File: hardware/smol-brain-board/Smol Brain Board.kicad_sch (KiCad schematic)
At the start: 59 parts, among them J1 USB4085-GF-A, J3 CAN_DBG, J6 Smol_Brain_Board, J7 PROGRAM, J8 Jumper 2Way Vert Solderable, J9 Jumper 2Way Vert Solderable, U1 ESP32-S3-WROOM-1-N8, U3 SN65HVD231D

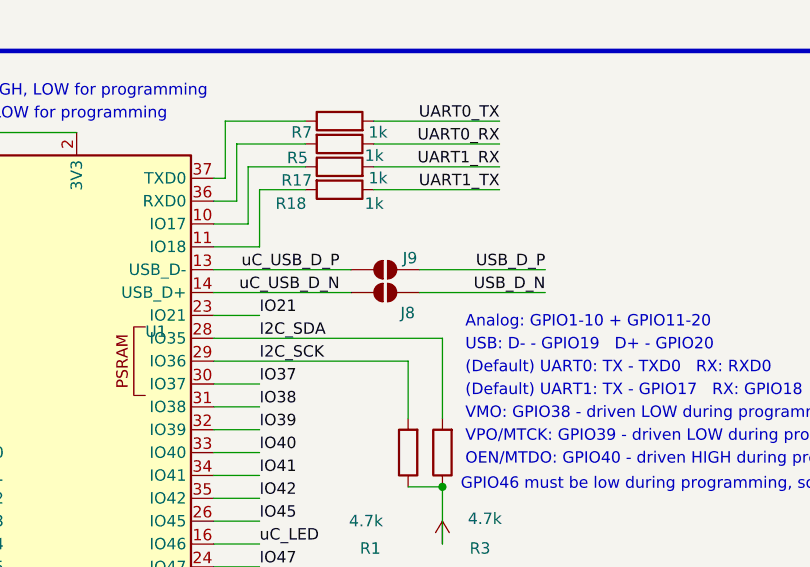
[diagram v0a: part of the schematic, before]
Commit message: Fixed impedance matching for USB and decoupling cap placement
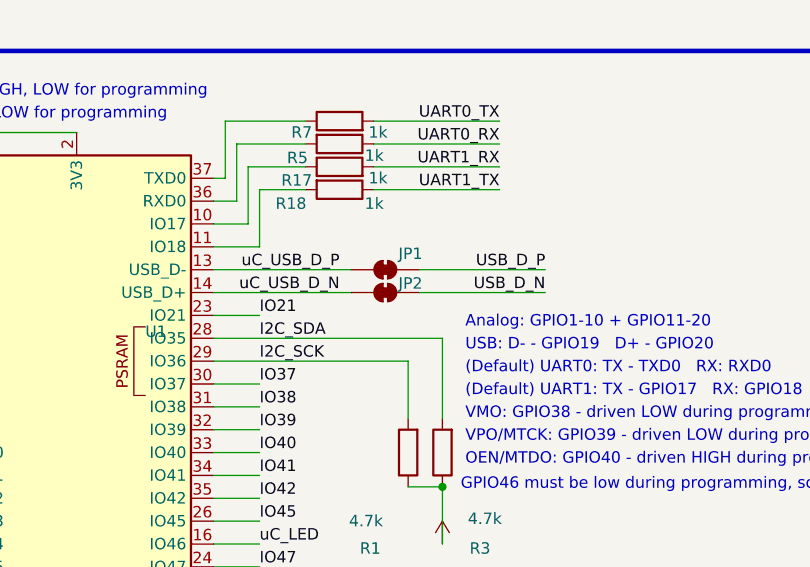
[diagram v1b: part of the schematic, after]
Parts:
- removed J8, J9: Jumper 2Way Vert Solderable, Jumper:SolderJumper-2_P1.3mm_Open_RoundedPad1.0x1.5mm, symbol Jumper:SolderJumper_2_Open
- added JP1, JP2: SolderJumper_2_Bridged, Jumper:SolderJumper-2_P1.3mm_Bridged_RoundedPad1.0x1.5mm, symbol Jumper:SolderJumper_2_Bridged
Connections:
- net USB_D_N: now also JP2.2 (B)
- net USB_D_P: now also JP1.2 (B)
- net uC_USB_D_N: now also JP2.1 (A)
- net uC_USB_D_P: now also JP1.1 (A)
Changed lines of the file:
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@@
 	(label "USB_D_N"
 		(at 359.41 48.26 180)
+		(fields_autoplaced yes)
 		(effects
 			(font
@@
 			(justify right bottom)
 		)
+		(property "Netclass" "USB_DIFF"
+			(at 359.41 49.53 0)
+			(effects
+				(font
+					(size 1.27 1.27)
+					(italic yes)
+				)
+				(justify right)
+				(hide yes)
+			)
+		)
 	)
 	(label "CAN_TX"
@@
 			(justify right bottom)
 		)
+		(property "Netclass" "USB_DIFF"
+			(at 337.058 42.672 0)
+			(effects
+				(font
+					(size 1.27 1.27)
+					(italic yes)
+				)
+				(justify right)
+				(hide yes)
+			)
+		)
 	)
 	(label "IO40"
@@
 	(label "USB_D_N"
 		(at 168.91 74.93 0)
+		(fields_autoplaced yes)
 		(effects
 			(font
@@
 			(justify left bottom)
 		)
+		(property "Netclass" "USB_DIFF"
+			(at 168.91 76.2 0)
+			(effects
+				(font
+					(size 1.27 1.27)
+					(italic yes)
+				)
+				(justify left)
+			)
+		)
 	)
 	(label "A4"
@@
 	(label "USB_D_P"
 		(at 359.41 45.72 180)
+		(fields_autoplaced yes)
 		(effects
 			(font
@@
 			(justify right bottom)
 		)
+		(property "Netclass" "USB_DIFF"
+			(at 359.41 46.99 0)
+			(effects
+				(font
+					(size 1.27 1.27)
+					(italic yes)
+				)
+				(justify right)
+				(hide yes)
+			)
+		)
 	)
 	(label "RST"
@@
 	(label "uC_USB_D_N"
 		(at 336.55 48.26 180)
+		(fields_autoplaced yes)
 		(effects
 			(font
@@
 			(justify right bottom)
 		)
+		(property "Netclass" "USB_DIFF"
+			(at 336.55 49.53 0)
+			(effects
+				(font
+					(size 1.27 1.27)
+					(italic yes)
+				)
+				(justify right)
+				(hide yes)
+			)
+		)
 	)
 	(label "CAN_H"
@@
 	(label "USB_D_P"
 		(at 168.91 80.01 0)
+		(fields_autoplaced yes)
 		(effects
 			(font
@@
 			(justify left bottom)
 		)
+		(property "Netclass" "USB_DIFF"
+			(at 168.91 81.28 0)
+			(effects
+				(font
+					(size 1.27 1.27)
+					(italic yes)
+				)
+				(justify left)
+			)
+		)
 	)
 	(label "IO15"
@@
 	)
 	(symbol
-		(lib_id "Jumper:SolderJumper_2_Open")
-		(at 341.63 45.72 180)
-		(unit 1)
-		(exclude_from_sim no)
-		(in_bom no)
-		(on_board yes)
-		(dnp no)
-		(property "Reference" "J9"
-			(at 345.186 43.688 0)
-			(effects
-				(font
-					(size 1.27 1.27)
-				)
-				(justify left bottom)
-			)
-		)
-		(property "Value" "Jumper 2Way Vert Solderable"
-			(at 349.758 46.99 0)
-			(effects
-				(font
-					(size 1.27 1.27)
-				)
-				(justify left bottom)
-				(hide yes)
-			)
-		)
-		(property "Footprint" "Jumper:SolderJumper-2_P1.3mm_Open_RoundedPad1.0x1.5mm"
-			(at 341.63 45.72 0)
-			(effects
-				(font
-					(size 1.27 1.27)
-				)
-				(hide yes)
-			)
-		)
-		(property "Datasheet" "~"
-			(at 341.63 45.72 0)
-			(effects
-				(font
-					(size 1.27 1.27)
-				)
-				(hide yes)
-			)
-		)
-		(property "Description" "Solder Jumper, 2-pole, open"
-			(at 341.63 45.72 0)
-			(effects
-				(font
-					(size 1.27 1.27)
-				)
-				(hide yes)
-			)
-		)
-		(property "SOURCE" "QUTMS_JumperLibrary.SchLib"
-			(at 349.758 46.99 0)
-			(effects
-				(font
-					(size 1.27 1.27)
-				)
-				(justify left bottom)
-				(hide yes)
-			)
-		)
-		(property "DESIGN ITEM ID" "Jumper 2Way Vert Solderable"
-			(at 349.758 46.99 0)
-			(effects
-				(font
-					(size 1.27 1.27)
-				)
-				(justify left bottom)
-				(hide yes)
-			)
-		)
-		(pin "1"
-		)
-		(pin "2"
-		)
-		(instances
-			(project ""
-				(path "/d947cca5-df2f-4130-8179-c021102beaa2"
-					(reference "J9")
-					(unit 1)
-				)
-			)
-		)
-	)
-	(symbol
 		(lib_id "power:GND")
 		(at 182.88 67.31 90)
@@
 	)
 	(symbol
-		(lib_id "Jumper:SolderJumper_2_Open")
-		(at 341.63 48.26 180)
+		(lib_id "Jumper:SolderJumper_2_Bridged")
+		(at 341.63 48.26 0)
 		(unit 1)
 		(exclude_from_sim no)
@@
 		(on_board yes)
 		(dnp no)
-		(property "Reference" "J8"
-			(at 344.932 49.784 0)
+		(property "Reference" "JP2"
+			(at 344.424 47.244 0)
 			(effects
 				(font
 					(size 1.27 1.27)
 				)
-				(justify left bottom)
 			)
 		)
-		(property "Value" "Jumper 2Way Vert Solderable"
-			(at 349.758 49.53 0)
+		(property "Value" "SolderJumper_2_Bridged"
+			(at 341.63 44.45 0)
 			(effects
 				(font
 					(size 1.27 1.27)
 				)
-				(justify left bottom)
 				(hide yes)
 			)
 		)
-		(property "Footprint" "Jumper:SolderJumper-2_P1.3mm_Open_RoundedPad1.0x1.5mm"
+		(property "Footprint" "Jumper:SolderJumper-2_P1.3mm_Bridged_RoundedPad1.0x1.5mm"
 			(at 341.63 48.26 0)
 			(effects
@@
 			)
 		)
-		(property "Description" "Solder Jumper, 2-pole, open"
+		(property "Description" "Solder Jumper, 2-pole, closed/bridged"
 			(at 341.63 48.26 0)
 			(effects
@@
 			)
 		)
-		(property "SOURCE" "QUTMS_JumperLibrary.SchLib"
-			(at 349.758 49.53 0)
-			(effects
-				(font
-					(size 1.27 1.27)
-				)
-				(justify left bottom)
-				(hide yes)
-			)
-		)
-		(property "DESIGN ITEM ID" "Jumper 2Way Vert Solderable"
-			(at 349.758 49.53 0)
-			(effects
-				(font
-					(size 1.27 1.27)
-				)
-				(justify left bottom)
-				(hide yes)
-			)
+		(pin "2"
 		)
 		(pin "1"
 		)
-		(pin "2"
-		)
 		(instances
-			(project ""
+			(project "Smol Brain Board"
 				(path "/d947cca5-df2f-4130-8179-c021102beaa2"
-					(reference "J8")
+					(reference "JP2")
 					(unit 1)
 				)
@@
 					(unit 1)
 				)
+			)
+		)
+	)
+	(symbol
+		(lib_id "Jumper:SolderJumper_2_Bridged")
+		(at 341.63 45.72 0)
+		(unit 1)
+		(exclude_from_sim no)
+		(in_bom no)
+		(on_board yes)
+		(dnp no)
+		(property "Reference" "JP1"
+			(at 344.424 43.942 0)
+			(effects
+				(font
+					(size 1.27 1.27)
+				)
+			)
+		)
+		(property "Value" "SolderJumper_2_Bridged"
+			(at 341.63 41.91 0)
+			(effects
+				(font
+					(size 1.27 1.27)
+				)
+				(hide yes)
+			)
+		)
+		(property "Footprint" "Jumper:SolderJumper-2_P1.3mm_Bridged_RoundedPad1.0x1.5mm"
+			(at 341.63 45.72 0)
+			(effects
+				(font
+					(size 1.27 1.27)
+				)
+				(hide yes)
+			)
+		)
+		(property "Datasheet" "~"
+			(at 341.63 45.72 0)
+			(effects
+				(font
+					(size 1.27 1.27)
+				)
+				(hide yes)
+			)
+		)
+		(property "Description" "Solder Jumper, 2-pole, closed/bridged"
+			(at 341.63 45.72 0)
+			(effects
+				(font
+					(size 1.27 1.27)
+				)
+				(hide yes)
+			)
+		)
+		(pin "2"
+		)
+		(pin "1"
+		)
+		(instances
+			(project ""
+				(path "/d947cca5-df2f-4130-8179-c021102beaa2"
+					(reference "JP1")
+					(unit 1)
+				)

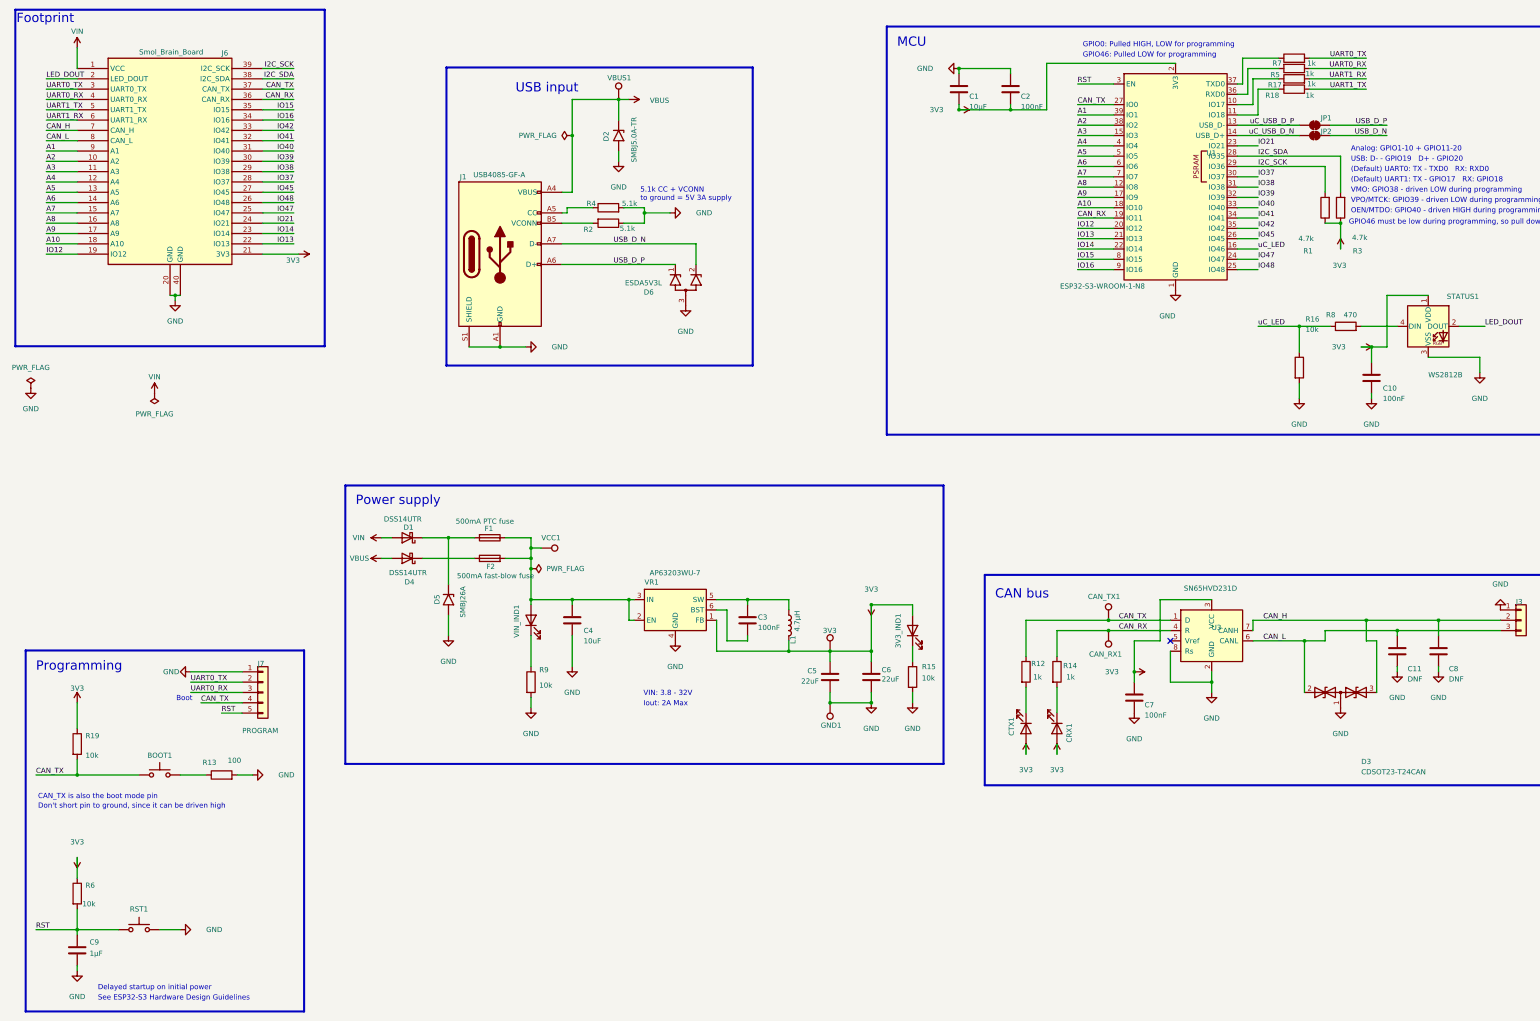
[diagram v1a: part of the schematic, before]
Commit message: Added real world components and finalised PCB, ready for manufacturing
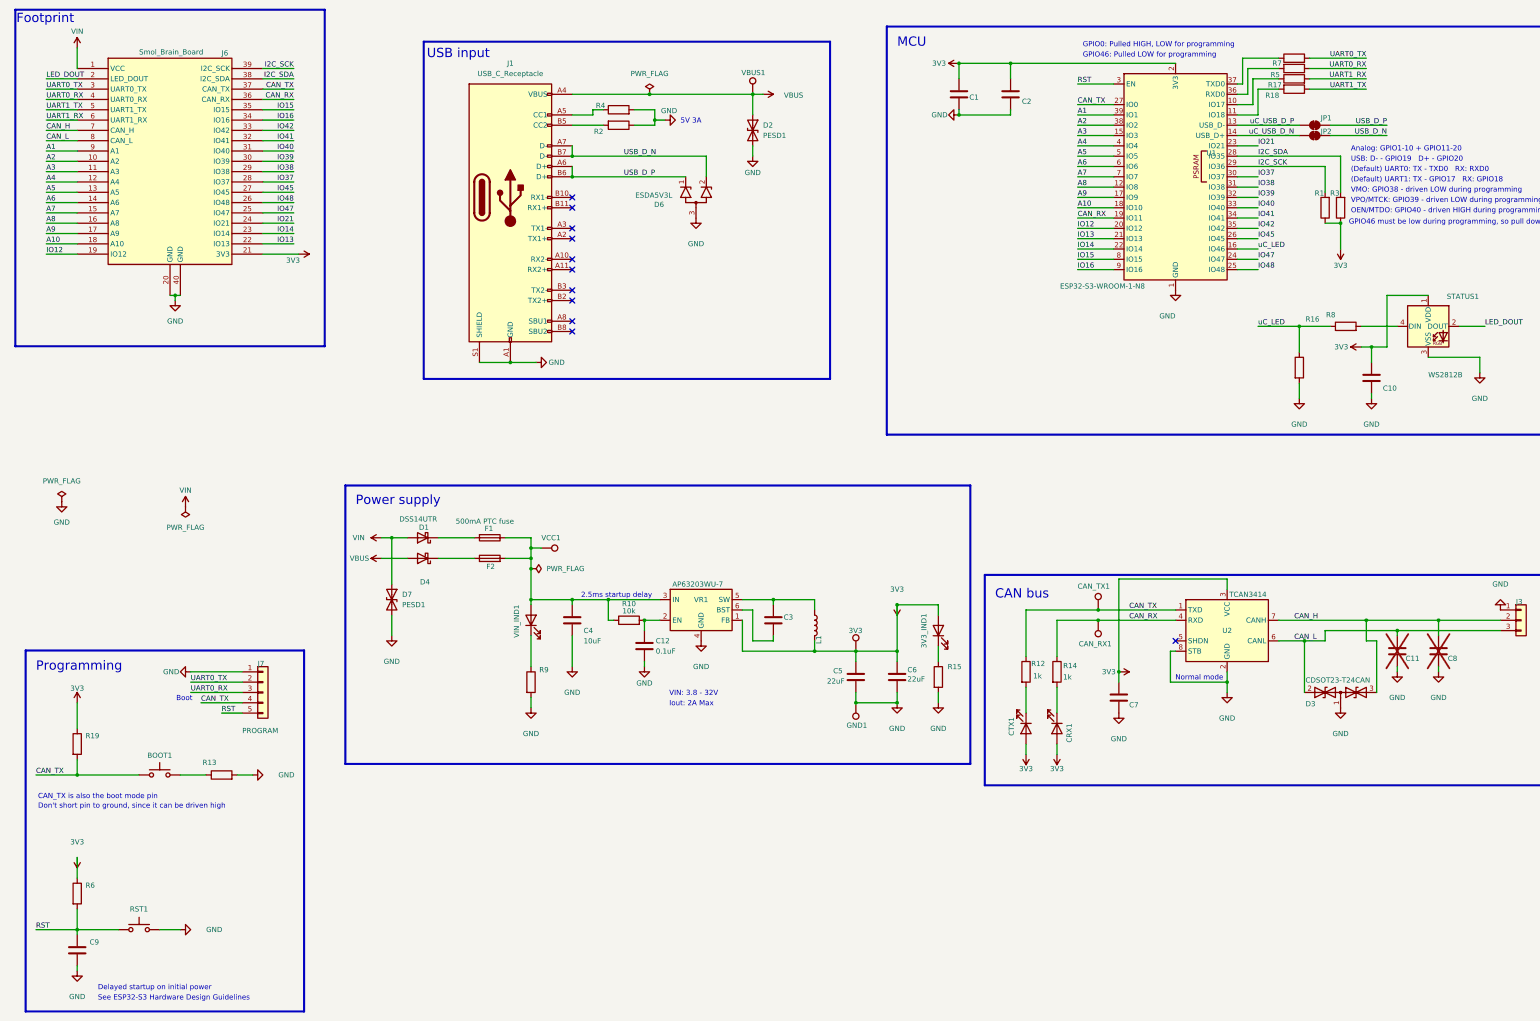
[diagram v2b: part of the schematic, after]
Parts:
- removed D2: SMBJ5.0A-TR, Diode_SMD:D_SMA, symbol Diode:SMAJ6.5A
- removed D5: SMBJ26A, Diode_SMD:D_SMA, symbol Diode:SMAJ26A
- removed J1: USB4085-GF-A, Connector_USB:USB_C_Receptacle_GCT_USB4085, symbol Connector:USB_C_Plug_USB2.0
- removed U3: SN65HVD231D, Package_SO:SOIC-8_3.9x4.9mm_P1.27mm, symbol Interface_CAN_LIN:SN65HVD231
- added C12: 0.1uF, Capacitor_SMD:C_0402_1005Metric, symbol Device:C
- added D2, D7: PESD1, Diode_SMD:D_SOD-882, symbol Device:D_TVS
- added J1: USB_C_Receptacle, Connector_USB:USB_C_Receptacle_Amphenol_12401610E4-2A, symbol Connector:USB_C_Receptacle
- added R10: 10k, Resistor_SMD:R_0402_1005Metric, symbol Device:R
- added U2: TCAN3414, Library:TCAN3414, symbol component_library:TCAN3414DDFR
- 3V3, CAN_RX1, CAN_TX1, GND1, VBUS1, VCC1: DESIGN ITEM ID Testpoint -> (none); SOURCE Testpoint.SchLib -> (none)
- 3V3_IND1, VIN_IND1: CASE/PACKAGE 0603 -> (none); COLOUR Red -> (none); DATASHEET URL http://optoelectronics.liteon.com/upload/download/DS-22-99-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 -> (none); DATASHEET VERSION Rev. F, 05/2013 -> (none); FORWARD CURRENT 20mA -> (none); FORWARD VOLTAGE 2V -> (none); ILLUMINATION COLOUR Red -> (none); LENS STYLE Diffused -> (none); LUMINOUS INTENSITY 54mcd -> (none); MANUFACTURER Lite-On -> (none); MANUFACTURER URL http://www.us.liteon.com/ -> (none); MAX OPERATING TEMPERATURE 85°C -> (none); MIN OPERATING TEMPERATURE -55°C -> (none); MOUNTING TECHNOLOGY SM -> (none); NOMINAL VF 2V -> (none); PACKAGE DESCRIPTION 2-Pin Surface Mount Device, Body 1.6 x 0.8 mm -> (none); PACKAGE QUANTITY 3000 -> (none); PACKAGE REFERENCE C191KRKT -> (none); PACKAGING TapeandReel -> (none); PINS 2 -> (none); POWER 75mW -> (none); ROHS COMPLIANT True -> (none); VIEWING ANGLE 130degrees -> (none); distributors part number (none) -> 160-1436-2-ND; manufactuer part number (none) -> LTST-C190KRKT; manufacturer (none) -> Lite-On Inc
- BOOT1, RST1: distributors part number (none) -> CKN12324-2-ND; manufactuer part number (none) -> GSPTS004302; manufacturer (none) -> C&K
- C1: ALTIUM_VALUE 10µF -> (none); CAPACITOR TYPE Ceramic -> (none); CASE/PACKAGE 0805 -> (none); DIELECTRIC MATERIAL Ceramic -> (none); HEIGHT 1.4mm -> (none); JESD-609 CODE e3 -> (none); LENGTH 2mm -> (none); MAX OPERATING TEMPERATURE 85°C -> (none); MIN OPERATING TEMPERATURE -55°C -> (none); MOUNTING TECHNOLOGY Surface Mount -> (none); MULTILAYER Yes -> (none); PACKAGE SHAPE Rectangular -> (none); PACKAGE STYLE SMTMeter -> (none); PACKAGING Tape and Reel -> (none); PINS 2 -> (none); RATED DC VOLTAGE (URDC) 16V -> (none); REACH SVHC COMPLIANT Yes -> (none); ROHS COMPLIANT Yes -> (none); TEMPERATURE CHARACTERISTICS CODE X5R -> (none); TERMINAL FINISH Nickel -> (none); TERMINATION Wraparound -> (none); TOLERANCE  (FILL IN AS +-) 10% -> (none); TOLERANCE (FILL IN AS +-) 10% -> (none); VOLTAGE RATING 16V -> (none); WIDTH 1.25mm -> (none); distributors part number (none) -> 1276-2872-2-ND; manufactuer part number (none) -> CL21B106KOQNNNE; manufacturer (none) -> Samsung Electro-Mechanics
- C10, C2, C3, C7: ALTIUM_VALUE 100nF -> (none); CAPACITOR TYPE Ceramic -> (none); CASE/PACKAGE 0603 -> (none); DIELECTRIC MATERIAL Ceramic -> (none); JESD-609 CODE e3 -> (none); MAX OPERATING TEMPERATURE 125°C -> (none); MIN OPERATING TEMPERATURE -55°C -> (none); MOUNTING TECHNOLOGY Surface Mount -> (none); MULTILAYER Yes -> (none); PACKAGE SHAPE Rectangular -> (none); PACKAGING Tape and Reel -> (none); PINS 2 -> (none); RATED DC VOLTAGE (URDC) 50V -> (none); REACH SVHC COMPLIANT Yes -> (none); ROHS COMPLIANT Yes -> (none); TEMPERATURE CHARACTERISTICS CODE X7R -> (none); TERMINAL FINISH Nickel -> (none); TERMINATION Wraparound -> (none); TOLERANCE  (FILL IN AS +-) 10% -> (none); TOLERANCE (FILL IN AS +-) 10% -> (none); VOLTAGE RATING 50V -> (none); distributors part number (none) -> 1276-1012-2-ND; manufactuer part number (none) -> CL10F104ZB8NNNC; manufacturer (none) -> Samsung Electro-Mechanics
- C11, C8: CAPACITOR TYPE Ceramic -> (none); CASE/PACKAGE 0603 -> (none); DNF DNF -> (none); MAX OPERATING TEMPERATURE 85°C -> (none); MIN OPERATING TEMPERATURE -55°C -> (none); MOUNTING TECHNOLOGY Surface Mount -> (none); PINS 2 -> (none); now not fitted
- C4: CAPACITANCE 10uF -> (none); CASE/PACKAGE 0603 -> (none); MAX OPERATING TEMPERATURE 85°C -> (none); MIN OPERATING TEMPERATURE -55°C -> (none); MOUNT Surface Mount -> (none); PACKAGING Tape and Reel -> (none); TOLERANCE 20% -> (none); VOLTAGE RATING 35V -> (none); distributors part number (none) -> 1276-1192-2-ND; manufactuer part number (none) -> CL10A106KP8NNNC; manufacturer (none) -> Samsung Electro-Mechanics
- C5, C6: CAPACITANCE 22uF -> (none); CASE CODE (IMPERIAL) 0805 -> (none); CASE CODE (METRIC) 2012 -> (none); CASE/PACKAGE 0805 -> (none); CONTACT PLATING Tin -> (none); DEPTH 1.25mm -> (none); DIELECTRIC X5R -> (none); HEIGHT 1.25mm -> (none); LEAD FREE Lead Free -> (none); LENGTH 2mm -> (none); MAX OPERATING TEMPERATURE 85°C -> (none); MIN OPERATING TEMPERATURE -55°C -> (none); MOUNT Surface Mount -> (none); PACKAGE QUANTITY 2000 -> (none); PACKAGING Tape and Reel -> (none); RADIATION HARDENING No -> (none); THICKNESS 0.055inch -> (none); TOLERANCE 20% -> (none); VOLTAGE RATING 6.3V -> (none); VOLTAGE RATING (DC) 6.3V -> (none); WIDTH 0.049inch -> (none); distributors part number (none) -> 1276-1274-2-ND; manufactuer part number (none) -> CL10A226MP8NUNE; manufacturer (none) -> Samsung Electro-Mechanics
- C9: value Capacitor 1u 25V 0603 -> Capacitor 1u 25V; ALTIUM_VALUE 1µF -> (none); CAPACITOR TYPE Ceramic -> (none); CASE/PACKAGE 0603 -> (none); DIELECTRIC MATERIAL Ceramic -> (none); HEIGHT 0.9mm -> (none); JESD-609 CODE e3 -> (none); LENGTH 1.6mm -> (none); MAX OPERATING TEMPERATURE 85°C -> (none); MIN OPERATING TEMPERATURE -55°C -> (none); MOUNTING TECHNOLOGY Surface Mount -> (none); MULTILAYER Yes -> (none); PACKAGE SHAPE Rectangular -> (none); PACKAGE STYLE SMTMeter -> (none); PACKAGING Tape and Reel -> (none); PINS 2 -> (none); RATED DC VOLTAGE (URDC) 25V -> (none); REACH SVHC COMPLIANT Yes -> (none); ROHS COMPLIANT Yes -> (none); TEMPERATURE CHARACTERISTICS CODE X5R -> (none); TERMINAL FINISH Nickel -> (none); TERMINATION Wraparound -> (none); TOLERANCE  (FILL IN AS +-) 10% -> (none); TOLERANCE (FILL IN AS +-) 10% -> (none); WIDTH 0.8mm -> (none); distributors part number (none) -> 1276-1184-2-ND; manufactuer part number (none) -> CL10B105KA8NNNC; manufacturer (none) -> Samsung Electro-Mechanics
- CRX1: footprint LED_SMD:LED_0603_1608Metric -> LED_SMD:LED_0402_1005Metric; CASE/PACKAGE 0603 -> (none); COLOUR Green -> (none); DATASHEET URL http://datasheet.octopart.com/LTST-C190GKT-Lite-On-datashee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 -> (none); DATASHEET VERSION Dec-06 -> (none); FORWARD CURRENT 20mA -> (none); FORWARD VOLTAGE 2.1V -> (none); ILLUMINATION COLOUR Green -> (none); LENS STYLE Clear -> (none); LUMINOUS INTENSITY 6mcd -> (none); MANUFACTURER Lite-On -> (none); MANUFACTURER URL http://www.us.liteon.com/ -> (none); MAX OPERATING TEMPERATURE 85°C -> (none); MIN OPERATING TEMPERATURE -55°C -> (none); MOUNTING TECHNOLOGY SM -> (none); NOMINAL VF 2.1V -> (none); PACKAGE DESCRIPTION 2-Pin Surface Mount Device, Body 1.6 x 0.8 mm -> (none); PACKAGE QUANTITY 3000 -> (none); PACKAGE REFERENCE C190GKT -> (none); PACKAGING TapeandReel -> (none); PINS 2 -> (none); POWER 100mW -> (none); ROHS COMPLIANT True -> (none); VIEWING ANGLE 130degrees -> (none); distributors part number (none) -> 160-1436-2-ND; manufactuer part number (none) -> LTST-C190KRKT; manufacturer (none) -> Lite-On Inc
- CTX1: footprint LED_SMD:LED_0603_1608Metric -> LED_SMD:LED_0402_1005Metric; CASE/PACKAGE 0603 -> (none); COLOUR Yellow -> (none); DATASHEET URL http://optoelectronics.liteon.com/upload/download/DS-22-99-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 -> (none); DATASHEET VERSION Rev. I, 10/2012 -> (none); FORWARD CURRENT 20mA -> (none); FORWARD VOLTAGE 2V -> (none); ILLUMINATION COLOUR Yellow -> (none); LENS STYLE Diffused -> (none); LUMINOUS INTENSITY 28mcd -> (none); MANUFACTURER Lite-On -> (none); MANUFACTURER URL http://www.us.liteon.com/ -> (none); MAX OPERATING TEMPERATURE 85°C -> (none); MIN OPERATING TEMPERATURE -55°C -> (none); MOUNTING TECHNOLOGY SM -> (none); NOMINAL VF 2.1V -> (none); PACKAGE DESCRIPTION 2-Pin Surface Mount Device, Body 1.6 x 0.8 mm -> (none); PACKAGE QUANTITY 3000 -> (none); PACKAGE REFERENCE C190KSKT -> (none); PACKAGING TapeandReel -> (none); PINS 2 -> (none); POWER 75mW -> (none); ROHS COMPLIANT True -> (none); VIEWING ANGLE 130degrees -> (none); distributors part number (none) -> 160-1436-2-ND; manufactuer part number (none) -> LTST-C190KRKT; manufacturer (none) -> Lite-On Inc
- D1, D4: ALTIUM_VALUE * -> (none); AVAILABILITY In Stock -> (none); CASE/PACKAGE SOD-123F SMC Diode Solutions -> (none); CHECK_PRICES https://www.snapeda.com/parts/DSS14UTR/SMC+Diode+Solutions/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 -> (none); DESIGN ITEM ID DSS14UTR -> (none); MF SMC Diode Solutions -> (none); MP DSS14UTR -> (none); PRICE None -> (none); PURCHASE-URL https://pricing.snapeda.com/search/part/DSS14UTR/?ref=eda -> (none); SNAPEDA_LINK https://www.snapeda.com/parts/DSS14UTR/SMC+Diode+Solutions/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 -> (none); SOURCE DSS14UTR.SchLib -> (none); distributors part number (none) -> 1655-DSS14UTR-ND; manufactuer part number (none) -> DSS14U; manufacturer (none) -> SMC Diode Solutions
- D3: ALTIUM_VALUE 22pF -> (none); AUTOMOTIVE No -> (none); BREAKDOWN VOLTAGE 26.2V -> (none); CAPACITANCE 22pF -> (none); CATEGORY Diode -> (none); CLAMPING VOLTAGE 40V -> (none); COMPONENTLINK2DESCRIPTION Datasheet -> (none); COMPONENTLINK2URL https://bourns.com/data/global/pdfs/CDSOT23-T24CAN.pdf -> (none); DEVICE CLASS L1 Circuit Protection -> (none); DEVICE CLASS L2 TVS Diodes -> (none); DEVICE CLASS L3 unset -> (none); DIGIKEY DESCRIPTION TVS DIODE 24V 40V SOT23 -> (none); DIRECTION Bidirectional -> (none); HEIGHT 1.17mm -> (none); IPC LAND PATTERN NAME SOT95P229X103-3 -> (none); LEAD FREE Yes -> (none); MANUFACTURER Bourns -> (none); MANUFACTURER PART NUMBER CDSOT23-T24CAN -> (none); MAX JUNCTION TEMP +150°C -> (none); MOUSER DESCRIPTION TVS Diodes / ESD Suppressors SOT-23 24V CANbus -> (none); NUMBER OF CHANNELS 2 -> (none); OCTOPART https://octopart.com/cdsot23-t24can-bourns-64883656 -> (none); PACKAGE SOT-23-3L -> (none); PEAK PULSE CURRENT 6A -> (none); ROHS TRUE -> (none); STANDOFF HEIGHT 0.05mm -> (none); TEMPERATURE -40°C to +150°C -> (none); TEMPERATURE RANGE HIGH +150°C -> (none); TEMPERATURE RANGE LOW -40°C -> (none); distributors part number (none) -> CDSOT23-T24CANTR-ND; manufactuer part number (none) -> CDSOT23-T24CAN; manufacturer (none) -> Bourns Inc.
- D6: ALTIUM_VALUE 220pF -> (none); AUTOMOTIVE No -> (none); BREAKDOWN VOLTAGE 5.3V -> (none); CAPACITANCE 220pF -> (none); CATEGORY Diode -> (none); COMPONENTLINK2DESCRIPTION Datasheet -> (none); COMPONENTLINK2URL https://www.st.com/content/ccc/resource/technical/document/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 -> (none); DEVICE CLASS L1 Circuit Protection -> (none); DEVICE CLASS L2 TVS Diodes -> (none); DEVICE CLASS L3 unset -> (none); DIGIKEY DESCRIPTION TVS DIODE 3V SOT23-3 -> (none); DIRECTION Unidirectional -> (none); HEIGHT 1.4mm -> (none); IPC LAND PATTERN NAME SOT95P255X115-3 -> (none); LEAD FREE Yes -> (none); MANUFACTURER STMicroelectronics -> (none); MANUFACTURER PART NUMBER ESDA5V3L -> (none); MAX JUNCTION TEMP +150°C -> (none); MOUSER DESCRIPTION ESDA Series 2 Channel 5.3 V 220 pF SMT Uni-Directional Tran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 -> (none); NUMBER OF CHANNELS 2 -> (none); OCTOPART https://octopart.com/esda5v3l-stmicroelectronics-347708 -> (none); PACKAGE SOT23-3L-0053390 -> (none); PEAK PULSE CURRENT 25A -> (none); PEAK PULSE POWER 300W -> (none); REVERSE STANDOFF VOLTAGE 3V -> (none); ROHS TRUE -> (none); STANDOFF HEIGHT 0mm -> (none); TEMPERATURE -40°C to +150°C -> (none); TEMPERATURE RANGE HIGH +150°C -> (none); TEMPERATURE RANGE LOW -40°C -> (none); distributors part number (none) -> 497-6632-2-ND; manufactuer part number (none) -> ESDA5V3L; manufacturer (none) -> STMicroelectronics
- F1: CASE/PACKAGE 1812 -> (none); CURRENT RATING 500mA -> (none); MAX OPERATING TEMPERATURE 85°C -> (none); MIN OPERATING TEMPERATURE -45°C -> (none); PINS 2 -> (none); distributors part number (none) -> 13-SMD1812B050TF/30TR-ND; manufactuer part number (none) -> SMD1812B050TF/30; manufacturer (none) -> YAGEO
- F2: ALTIUM_VALUE 232mΩ -> (none); AUTOMOTIVE No -> (none); CATEGORY Fuse -> (none); COMPONENTLINK2DESCRIPTION Datasheet -> (none); COMPONENTLINK2URL https://www.bourns.com/docs/product-datasheets/sf0603s.pdf -> (none); DEVICE CLASS L1 Circuit Protection -> (none); DEVICE CLASS L2 Fuses -> (none); DEVICE CLASS L3 unset -> (none); DIGIKEY DESCRIPTION FUSE BOARD MNT 500MA 50VDC 0603 -> (none); FUSE BLOW SPEED Slow -> (none); FUSE CURRENT 0.5A -> (none); FUSE I2T 0.009A2Sec -> (none); FUSE INTERRUPT AC CURRENT 50A -> (none); FUSE INTERRUPT DC CURRENT 50A -> (none); HEIGHT 0.55mm -> (none); IPC LAND PATTERN NAME CAPC16080X45 -> (none); LEAD FREE Yes -> (none); MANUFACTURER Bourns Inc. -> (none); MANUFACTURER PART NUMBER SF-0603S050-2 -> (none); MAX FUSE AC VOLTAGE 35V -> (none); MAX FUSE DC VOLTAGE 50V -> (none); MOUSER DESCRIPTION Surface Mount Fuses 0.50A Slow Blow SinglFuse -> (none); OCTOPART https://octopart.com/sf-0603s050-2-bourns-10486821 -> (none); PACKAGE SF-0603S -> (none); RESISTANCE 232mΩ -> (none); ROHS TRUE -> (none); TEMPERATURE -20°C to +105°C -> (none); TEMPERATURE RANGE HIGH +105°C -> (none); TEMPERATURE RANGE LOW -20°C -> (none); distributors part number (none) -> SF-0603S050-2TR-ND; manufactuer part number (none) -> SF-0603S050-2; manufacturer (none) -> Bourns Inc.
- J3: ALTIUM_VALUE Conn_01x03 -> (none); DESIGN ITEM ID Conn_01x03 -> (none); KI_DESCRIPTION Generic connector, single row, 01x03, script generated (kic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 -> (none); KI_FP_FILTERS Connector*:*_1x??_* -> (none); KI_KEYWORDS connector -> (none); SOURCE Connector_Generic.SchLib -> (none); distributors part number (none) -> 455-2248-ND; manufactuer part number (none) -> B3B-XH-A; manufacturer (none) -> JST Sales America Inc.
- J6: DESIGN ITEM ID Smol_Brain_Board -> (none); SOURCE QUTRC_ARC.SchLib -> (none)
- J7: ALTIUM_VALUE Conn_01x05 -> (none); DESIGN ITEM ID Conn_01x05 -> (none); KI_DESCRIPTION Generic connector, single row, 01x05, script generated (kic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 -> (none); KI_FP_FILTERS Connector*:*_1x??_* -> (none); KI_KEYWORDS connector -> (none); SOURCE Connector_Generic.SchLib -> (none)
- L1: ALTIUM_VALUE 4.7µH -> (none); CASE/PACKAGE 1616 -> (none); CURRENT RATING 2A -> (none); MAX CURRENT RATING 2A -> (none); MAX OPERATING TEMPERATURE 125°C -> (none); MIN OPERATING TEMPERATURE -40°C -> (none); PINS 2 -> (none); TOLERANCE 20% -> (none); distributors part number (none) -> 4816-HPC4018NF-4R7MTR-ND; manufactuer part number (none) -> HPC 4018NF-4R7M; manufacturer (none) -> TAI-TECH Advanced Electronics Co., Ltd.
- R1, R3: value Resistor 4.7k 0603 -> 4.7k; footprint Resistor_SMD:R_0201_0603Metric -> Resistor_SMD:R_0402_1005Metric; ALTIUM_VALUE 4.7k -> (none); CASE/PACKAGE 0603 -> (none); CONSTRUCTION Rectangular -> (none); JESD-609 CODE e3 -> (none); MAX OPERATING TEMPERATURE 155°C -> (none); MIN OPERATING TEMPERATURE -55°C -> (none); MOUNTING TECHNOLOGY Surface Mount -> (none); PACKAGE HEIGHT 0.45mm -> (none); PACKAGE LENGTH 1.55mm -> (none); PACKAGE SHAPE Rectangular -> (none); PACKAGE STYLE SMTMeter -> (none); PACKAGE WIDTH 0.8mm -> (none); PACKAGING Tape and Reel -> (none); PINS 2 -> (none); POWER 100mW -> (none); RATED TEMPERATURE 70°C -> (none); REACH SVHC COMPLIANT Yes -> (none); REFERENCE STANDARD AEC-Q200 -> (none); RESISTOR TYPE FIXED RESISTOR -> (none); ROHS COMPLIANT Yes -> (none); TECHNOLOGY METAL GLAZE/THICK FILM -> (none); TEMPERATURE COEFFICIENT 100ppm/°C -> (none); TERMINAL FINISH Nickel -> (none); TERMINATION Wraparound -> (none); TOLERANCE 1% -> (none); WORKING VOLTAGE 75V -> (none); distributors part number (none) -> 311-4.7KJRTR-ND; manufactuer part number (none) -> RC0402JR-074K7L; manufacturer (none) -> YAGEO
- R12, R14: value Resistor 1k 0603 -> 1k; footprint Resistor_SMD:R_0201_0603Metric -> Resistor_SMD:R_0402_1005Metric; ALTIUM_VALUE 1k -> (none); CASE/PACKAGE 0603 -> (none); CONSTRUCTION Rectangular -> (none); JESD-609 CODE e3 -> (none); MAX OPERATING TEMPERATURE 155°C -> (none); MIN OPERATING TEMPERATURE -55°C -> (none); MOUNTING TECHNOLOGY Surface Mount -> (none); PACKAGE HEIGHT 0.45mm -> (none); PACKAGE LENGTH 1.55mm -> (none); PACKAGE SHAPE Rectangular -> (none); PACKAGE STYLE SMTMeter -> (none); PACKAGE WIDTH 0.8mm -> (none); PACKAGING Tape and Reel -> (none); PINS 2 -> (none); POWER 100mW -> (none); RATED TEMPERATURE 70°C -> (none); REACH SVHC COMPLIANT Yes -> (none); REFERENCE STANDARD AEC-Q200 -> (none); RESISTOR TYPE FIXED RESISTOR -> (none); ROHS COMPLIANT Yes -> (none); TECHNOLOGY METAL GLAZE/THICK FILM -> (none); TEMPERATURE COEFFICIENT 100ppm/°C -> (none); TERMINAL FINISH Nickel -> (none); TERMINATION Wraparound -> (none); TOLERANCE 1% -> (none); WORKING VOLTAGE 75V -> (none); distributors part number (none) -> 311-1.0KJRTR-ND; manufactuer part number (none) -> RC0402JR-071KL; manufacturer (none) -> YAGEO
- R13: value Resistor 100R 0603 -> 100R; footprint Resistor_SMD:R_0201_0603Metric -> Resistor_SMD:R_0402_1005Metric; ALTIUM_VALUE 100 -> (none); CASE/PACKAGE 0603 -> (none); CONSTRUCTION Rectangular -> (none); JESD-609 CODE e3 -> (none); MAX OPERATING TEMPERATURE 155°C -> (none); MIN OPERATING TEMPERATURE -55°C -> (none); MOUNTING TECHNOLOGY Surface Mount -> (none); PACKAGE HEIGHT 0.45mm -> (none); PACKAGE LENGTH 1.55mm -> (none); PACKAGE SHAPE Rectangular -> (none); PACKAGE STYLE SMTMeter -> (none); PACKAGE WIDTH 0.8mm -> (none); PACKAGING Tape and Reel -> (none); PINS 2 -> (none); POWER 100mW -> (none); RATED TEMPERATURE 70°C -> (none); REACH SVHC COMPLIANT Yes -> (none); REFERENCE STANDARD AEC-Q200 -> (none); RESISTOR TYPE FIXED RESISTOR -> (none); ROHS COMPLIANT Yes -> (none); TECHNOLOGY METAL GLAZE/THICK FILM -> (none); TEMPERATURE COEFFICIENT 100ppm/°C -> (none); TERMINAL FINISH Nickel -> (none); TERMINATION Wraparound -> (none); TOLERANCE 1% -> (none); WORKING VOLTAGE 75V -> (none); distributors part number (none) -> 311-100LRTR-ND; manufactuer part number (none) -> RC0402FR-07100RL; manufacturer (none) -> YAGEO
- R15, R16, R9: footprint Resistor_SMD:R_0201_0603Metric -> Resistor_SMD:R_0603_1608Metric; ALTIUM_VALUE 10k -> (none); CASE/PACKAGE 0603 -> (none); CONSTRUCTION Rectangular -> (none); JESD-609 CODE e3 -> (none); MAX OPERATING TEMPERATURE 155°C -> (none); MIN OPERATING TEMPERATURE -55°C -> (none); MOUNTING TECHNOLOGY Surface Mount -> (none); PACKAGE HEIGHT 0.45mm -> (none); PACKAGE LENGTH 1.55mm -> (none); PACKAGE SHAPE Rectangular -> (none); PACKAGE STYLE SMTMeter -> (none); PACKAGE WIDTH 0.8mm -> (none); PACKAGING Tape and Reel -> (none); PINS 2 -> (none); POWER 100mW -> (none); RATED TEMPERATURE 70°C -> (none); REACH SVHC COMPLIANT Yes -> (none); REFERENCE STANDARD AEC-Q200 -> (none); RESISTOR TYPE FIXED RESISTOR -> (none); ROHS COMPLIANT Yes -> (none); TECHNOLOGY METAL GLAZE/THICK FILM -> (none); TEMPERATURE COEFFICIENT 100ppm/°C -> (none); TERMINAL FINISH Nickel -> (none); TERMINATION Wraparound -> (none); TOLERANCE 1% -> (none); WORKING VOLTAGE 75V -> (none); distributors part number (none) -> 311-10.0KHRTR-ND; manufactuer part number (none) -> RC0603FR-0710KL; manufacturer (none) -> YAGEO
- R17, R18: footprint Resistor_SMD:R_0201_0603Metric -> Resistor_SMD:R_0402_1005Metric; ALTIUM_VALUE 1k -> (none); CASE/PACKAGE 0603 -> (none); CONSTRUCTION Rectangular -> (none); JESD-609 CODE e3 -> (none); MAX OPERATING TEMPERATURE 155°C -> (none); MIN OPERATING TEMPERATURE -55°C -> (none); MOUNTING TECHNOLOGY Surface Mount -> (none); PACKAGE HEIGHT 0.45mm -> (none); PACKAGE LENGTH 1.55mm -> (none); PACKAGE SHAPE Rectangular -> (none); PACKAGE STYLE SMTMeter -> (none); PACKAGE WIDTH 0.8mm -> (none); PACKAGING Tape and Reel -> (none); PINS 2 -> (none); POWER 100mW -> (none); RATED TEMPERATURE 70°C -> (none); REACH SVHC COMPLIANT Yes -> (none); REFERENCE STANDARD AEC-Q200 -> (none); RESISTOR TYPE FIXED RESISTOR -> (none); ROHS COMPLIANT Yes -> (none); TECHNOLOGY METAL GLAZE/THICK FILM -> (none); TEMPERATURE COEFFICIENT 100ppm/°C -> (none); TERMINAL FINISH Nickel -> (none); TERMINATION Wraparound -> (none); TOLERANCE 1% -> (none); WORKING VOLTAGE 75V -> (none); distributors part number (none) -> 311-1.0KJRTR-ND; manufactuer part number (none) -> RC0402JR-071KL; manufacturer (none) -> YAGEO
- R19: footprint Resistor_SMD:R_0201_0603Metric -> Resistor_SMD:R_0402_1005Metric; ALTIUM_VALUE 10k -> (none); CASE/PACKAGE 0603 -> (none); CONSTRUCTION Rectangular -> (none); JESD-609 CODE e3 -> (none); MAX OPERATING TEMPERATURE 155°C -> (none); MIN OPERATING TEMPERATURE -55°C -> (none); MOUNTING TECHNOLOGY Surface Mount -> (none); PACKAGE HEIGHT 0.45mm -> (none); PACKAGE LENGTH 1.55mm -> (none); PACKAGE SHAPE Rectangular -> (none); PACKAGE STYLE SMTMeter -> (none); PACKAGE WIDTH 0.8mm -> (none); PACKAGING Tape and Reel -> (none); PINS 2 -> (none); POWER 100mW -> (none); RATED TEMPERATURE 70°C -> (none); REACH SVHC COMPLIANT Yes -> (none); REFERENCE STANDARD AEC-Q200 -> (none); RESISTOR TYPE FIXED RESISTOR -> (none); ROHS COMPLIANT Yes -> (none); TECHNOLOGY METAL GLAZE/THICK FILM -> (none); TEMPERATURE COEFFICIENT 100ppm/°C -> (none); TERMINAL FINISH Nickel -> (none); TERMINATION Wraparound -> (none); TOLERANCE 1% -> (none); WORKING VOLTAGE 75V -> (none); distributors part number (none) -> 311-10.0KHRTR-ND; manufactuer part number (none) -> RC0603FR-0710KL; manufacturer (none) -> YAGEO
- R2, R4: value Resistor 5.1k 0603 -> Resistor 5.1k; footprint Resistor_SMD:R_0201_0603Metric -> Resistor_SMD:R_0402_1005Metric; ALTIUM_VALUE 5.1k -> (none); CASE/PACKAGE 0603 -> (none); CONSTRUCTION Rectangular -> (none); JESD-609 CODE e3 -> (none); MAX OPERATING TEMPERATURE 155°C -> (none); MIN OPERATING TEMPERATURE -55°C -> (none); MOUNTING TECHNOLOGY Surface Mount -> (none); PACKAGE HEIGHT 0.45mm -> (none); PACKAGE LENGTH 1.55mm -> (none); PACKAGE SHAPE Rectangular -> (none); PACKAGE STYLE SMTMeter -> (none); PACKAGE WIDTH 0.8mm -> (none); PACKAGING Tape and Reel -> (none); PINS 2 -> (none); POWER 100mW -> (none); RATED TEMPERATURE 70°C -> (none); REACH SVHC COMPLIANT Yes -> (none); REFERENCE STANDARD AEC-Q200 -> (none); RESISTOR TYPE FIXED RESISTOR -> (none); ROHS COMPLIANT Yes -> (none); TECHNOLOGY METAL GLAZE/THICK FILM -> (none); TEMPERATURE COEFFICIENT 100ppm/°C -> (none); TERMINAL FINISH Nickel -> (none); TERMINATION Wraparound -> (none); TOLERANCE 1% -> (none); WORKING VOLTAGE 75V -> (none); distributors part number (none) -> 311-5.1KJRTR-ND; manufactuer part number (none) -> RC0402JR-075K1L; manufacturer (none) -> YAGEO
- R5, R7: footprint Resistor_SMD:R_0201_0603Metric -> Resistor_SMD:R_0603_1608Metric; ALTIUM_VALUE 1k -> (none); CASE/PACKAGE 0603 -> (none); CONSTRUCTION Rectangular -> (none); JESD-609 CODE e3 -> (none); MAX OPERATING TEMPERATURE 155°C -> (none); MIN OPERATING TEMPERATURE -55°C -> (none); MOUNTING TECHNOLOGY Surface Mount -> (none); PACKAGE HEIGHT 0.45mm -> (none); PACKAGE LENGTH 1.55mm -> (none); PACKAGE SHAPE Rectangular -> (none); PACKAGE STYLE SMTMeter -> (none); PACKAGE WIDTH 0.8mm -> (none); PACKAGING Tape and Reel -> (none); PINS 2 -> (none); POWER 100mW -> (none); RATED TEMPERATURE 70°C -> (none); REACH SVHC COMPLIANT Yes -> (none); REFERENCE STANDARD AEC-Q200 -> (none); RESISTOR TYPE FIXED RESISTOR -> (none); ROHS COMPLIANT Yes -> (none); TECHNOLOGY METAL GLAZE/THICK FILM -> (none); TEMPERATURE COEFFICIENT 100ppm/°C -> (none); TERMINAL FINISH Nickel -> (none); TERMINATION Wraparound -> (none); TOLERANCE 1% -> (none); WORKING VOLTAGE 75V -> (none); distributors part number (none) -> 311-1KMTR-ND; manufactuer part number (none) -> RC0201FR-071KL; manufacturer (none) -> YAGEO
- R6: value Resistor 10k 0603 -> 10k; footprint Resistor_SMD:R_0201_0603Metric -> Resistor_SMD:R_0402_1005Metric; ALTIUM_VALUE 10k -> (none); CASE/PACKAGE 0603 -> (none); CONSTRUCTION Rectangular -> (none); JESD-609 CODE e3 -> (none); MAX OPERATING TEMPERATURE 155°C -> (none); MIN OPERATING TEMPERATURE -55°C -> (none); MOUNTING TECHNOLOGY Surface Mount -> (none); PACKAGE HEIGHT 0.45mm -> (none); PACKAGE LENGTH 1.55mm -> (none); PACKAGE SHAPE Rectangular -> (none); PACKAGE STYLE SMTMeter -> (none); PACKAGE WIDTH 0.8mm -> (none); PACKAGING Tape and Reel -> (none); PINS 2 -> (none); POWER 100mW -> (none); RATED TEMPERATURE 70°C -> (none); REACH SVHC COMPLIANT Yes -> (none); REFERENCE STANDARD AEC-Q200 -> (none); RESISTOR TYPE FIXED RESISTOR -> (none); ROHS COMPLIANT Yes -> (none); TECHNOLOGY METAL GLAZE/THICK FILM -> (none); TEMPERATURE COEFFICIENT 100ppm/°C -> (none); TERMINAL FINISH Nickel -> (none); TERMINATION Wraparound -> (none); TOLERANCE 1% -> (none); WORKING VOLTAGE 75V -> (none); distributors part number (none) -> 1276-3431-2-ND; manufactuer part number (none) -> RC1005F103CS; manufacturer (none) -> Samsung Electro-Mechanics
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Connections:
- net 3V3: now also U2.3 (VCC)
- net CAN_H: now also U2.7 (CANH)
- net CAN_L: now also U2.6 (CANL)
- net CAN_RX: now also U2.4 (RXD)
- net CAN_TX: now also U2.1 (TXD)
- net GND: now also C12.2, D2.2 (A2), D7.2 (A2), J1.A1 (GND), J1.A12 (GND), J1.B1 (GND), J1.B12 (GND), J1.S1 (SHIELD), U2.2 (GND), U2.8 (STB)
- net USB_D_N: now also J1.A7 (D-), J1.B7 (D-)
- net USB_D_P: now also J1.A6 (D+), J1.B6 (D+)
- net VBUS: now also D2.1 (A1), J1.A4 (VBUS), J1.A9 (VBUS), J1.B4 (VBUS), J1.B9 (VBUS)
- net VIN: now also D7.1 (A1)
- net at C4.1, F1.1, F2.2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: now also R10.1; no longer VR1.2 (EN)
- net at R4.1: now also J1.A5 (CC1)
- net at R2.2: now also J1.B5 (CC2)
- new net: C12.1, R10.2, VR1.2 (EN)
- no-connect marks 1 -> 11
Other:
- note added: "2.5ms startup delay"
- note added: "5V 3A"
- note added: "Normal mode"
- note removed: "5.1k CC + VCONN to ground = 5V 3A supply"
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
